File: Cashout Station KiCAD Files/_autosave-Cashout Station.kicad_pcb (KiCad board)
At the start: 2 copper layers, 48 x 110 mm, 17 parts, among them J1 Audio Connecter, M1 Servo Connecter, M2 Servo Connecter, SW1 Le Button: The Sequel, SW2 Le Button, U1 XIAO-ESP32-C6, U2 Batt Step Down

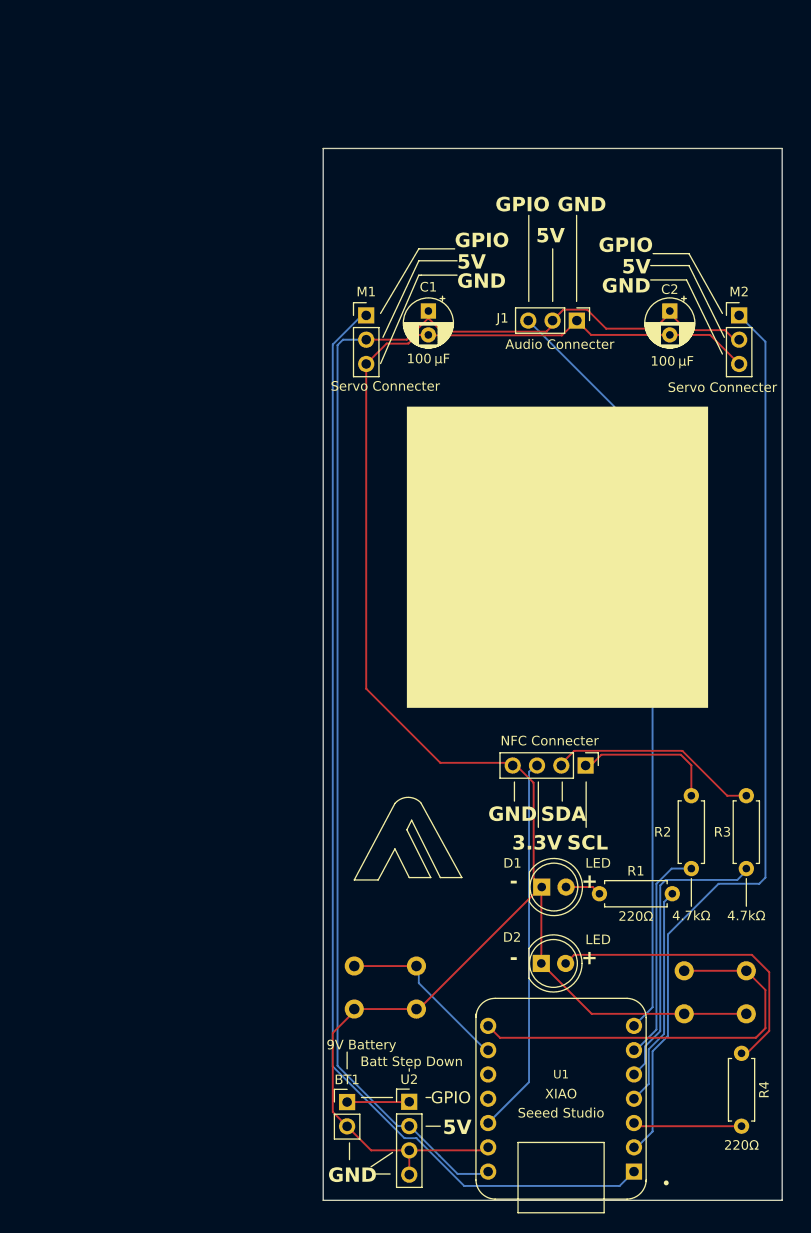
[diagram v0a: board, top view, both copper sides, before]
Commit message: PCB Updated, CAD almost complete
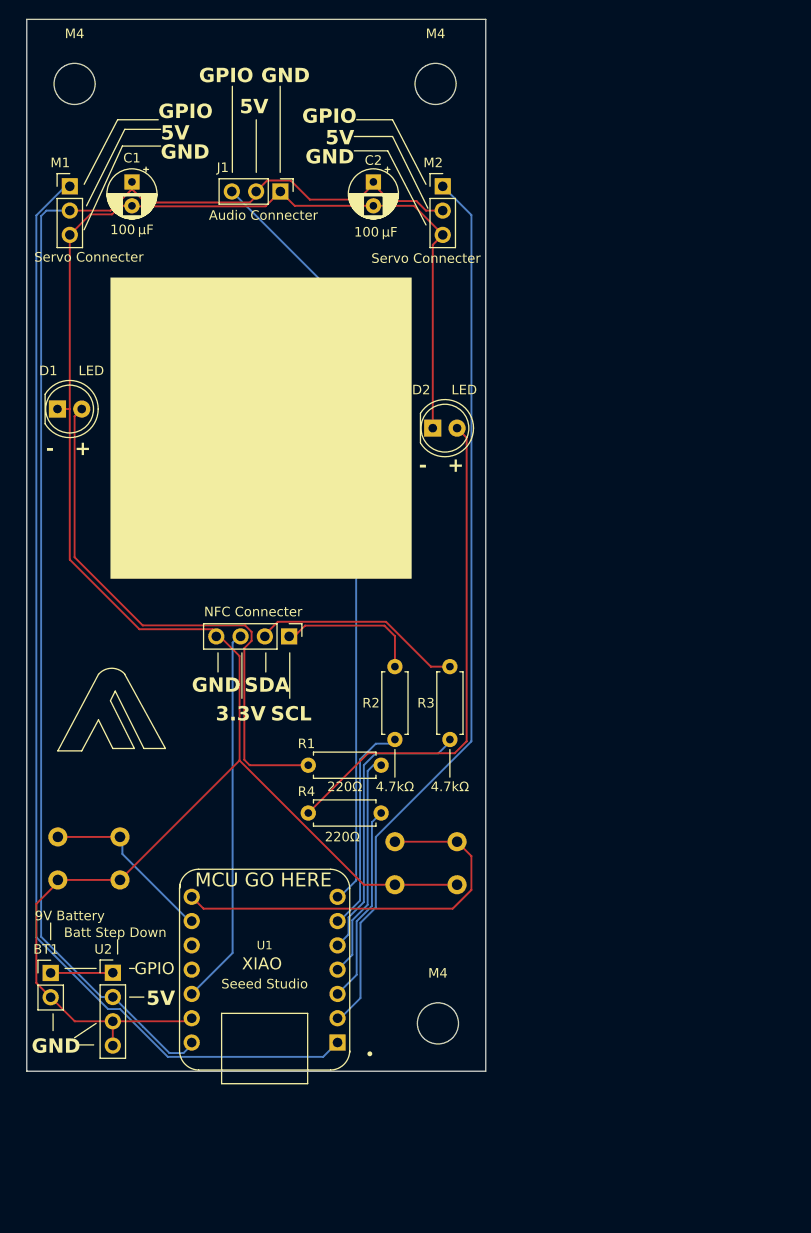
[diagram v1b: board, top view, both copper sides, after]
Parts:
- added M4: MountingHole_4.3mm_M4, MountingHole:MountingHole_4.3mm_M4, F.Cu at (124.0, 43.2)
- added M4: MountingHole_4.3mm_M4, MountingHole:MountingHole_4.3mm_M4, F.Cu at (162.0, 141.5)
- added M4: MountingHole_4.3mm_M4, MountingHole:MountingHole_4.3mm_M4, F.Cu at (161.8, 43.2)
- moved D1 71.2 mm to (122.2, 77.2)
- moved D2 57.1 mm to (161.5, 79.2)
- moved R4 51.8 mm to (148.4, 119.5), turned to 0 degrees
- moved BT1 33.8 mm to (121.5, 136.2)
- moved C1 33.8 mm to (130.0, 53.5)
- moved C2 33.8 mm to (155.2, 53.5)
- moved J1 33.8 mm to (145.5, 54.5)
- moved M1 33.8 mm to (123.5, 54.0)
- moved M2 33.8 mm to (162.5, 54.0)
- moved NFC Connecter 33.8 mm to (146.4, 101.0)
- moved R2 33.8 mm to (157.5, 111.8)
- moved R3 33.8 mm to (163.2, 111.8)
- moved SW2 33.8 mm to (128.8, 122.0)
- moved U1 33.8 mm to (143.9, 135.9)
- moved U2 33.8 mm to (128.0, 136.2)
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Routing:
- net Net-(D1-A): track 3.78 -> 58.2 mm
- net Net-(D2-A): track 32.7 -> 52.8 mm
- net GND: track 198.6 -> 216.4 mm
- net Net-(U1-GPIO2/A2/D2): track 11.4 -> 21.4 mm
- net Net-(M2-PWM): track 96.5 -> 94.2 mm
- net Net-(U1-GPIO21/D3): track 23.1 -> 23.7 mm
- net Net-(U1-GPIO22/D4/SDA): track 30.9 -> 30.3 mm
- net Net-(U1-GPIO17/D7/RX): track 43.3 -> 42.7 mm
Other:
- board text added: "XIAO"
